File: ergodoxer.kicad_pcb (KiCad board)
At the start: 2 copper layers, 207 x 174.1 mm, 113 parts, among them J1 USB_C_Receptacle, SW1 SW_Push, SW10 SW_Push, SW11 SW_Push, SW12 SW_Push, SW13 SW_Push, SW14 SW_Push, SW15 SW_Push, SW16 SW_Push, SW17 SW_Push, SW18 SW_Push, SW19 SW_Push, SW2 SW_Push, SW20 SW_Push, SW21 SW_Push, SW22 SW_Push, SW23 SW_Push, SW24 SW_Push, SW25 SW_Push, SW26 SW_Push, SW27 SW_Push, SW28 SW_Push, SW29 SW_Push, SW3 SW_Push, SW30 SW_Push, SW31 SW_Push, SW32 SW_Push, SW33 SW_Push, SW34 SW_Push, SW35 SW_Push, SW36 SW_Push, SW37 SW_Push, SW38 SW_Push, SW39 SW_Push, SW4 SW_Push, SW40 SW_Push, SW41 SW_Push, SW43 SW_Push, SW44 SW_Push, SW45 SW_Push, SW46 SW_Push, SW47 SW_Push, SW48 SW_Push, SW49 SW_Push, SW5 SW_Push, SW50 SW_Push, SW51 SW_Push, SW52 SW_Push, SW53 SW_Push, SW6 SW_Push, SW7 SW_Push, SW8 SW_Push, SW9 SW_Push, U1 Proton_C

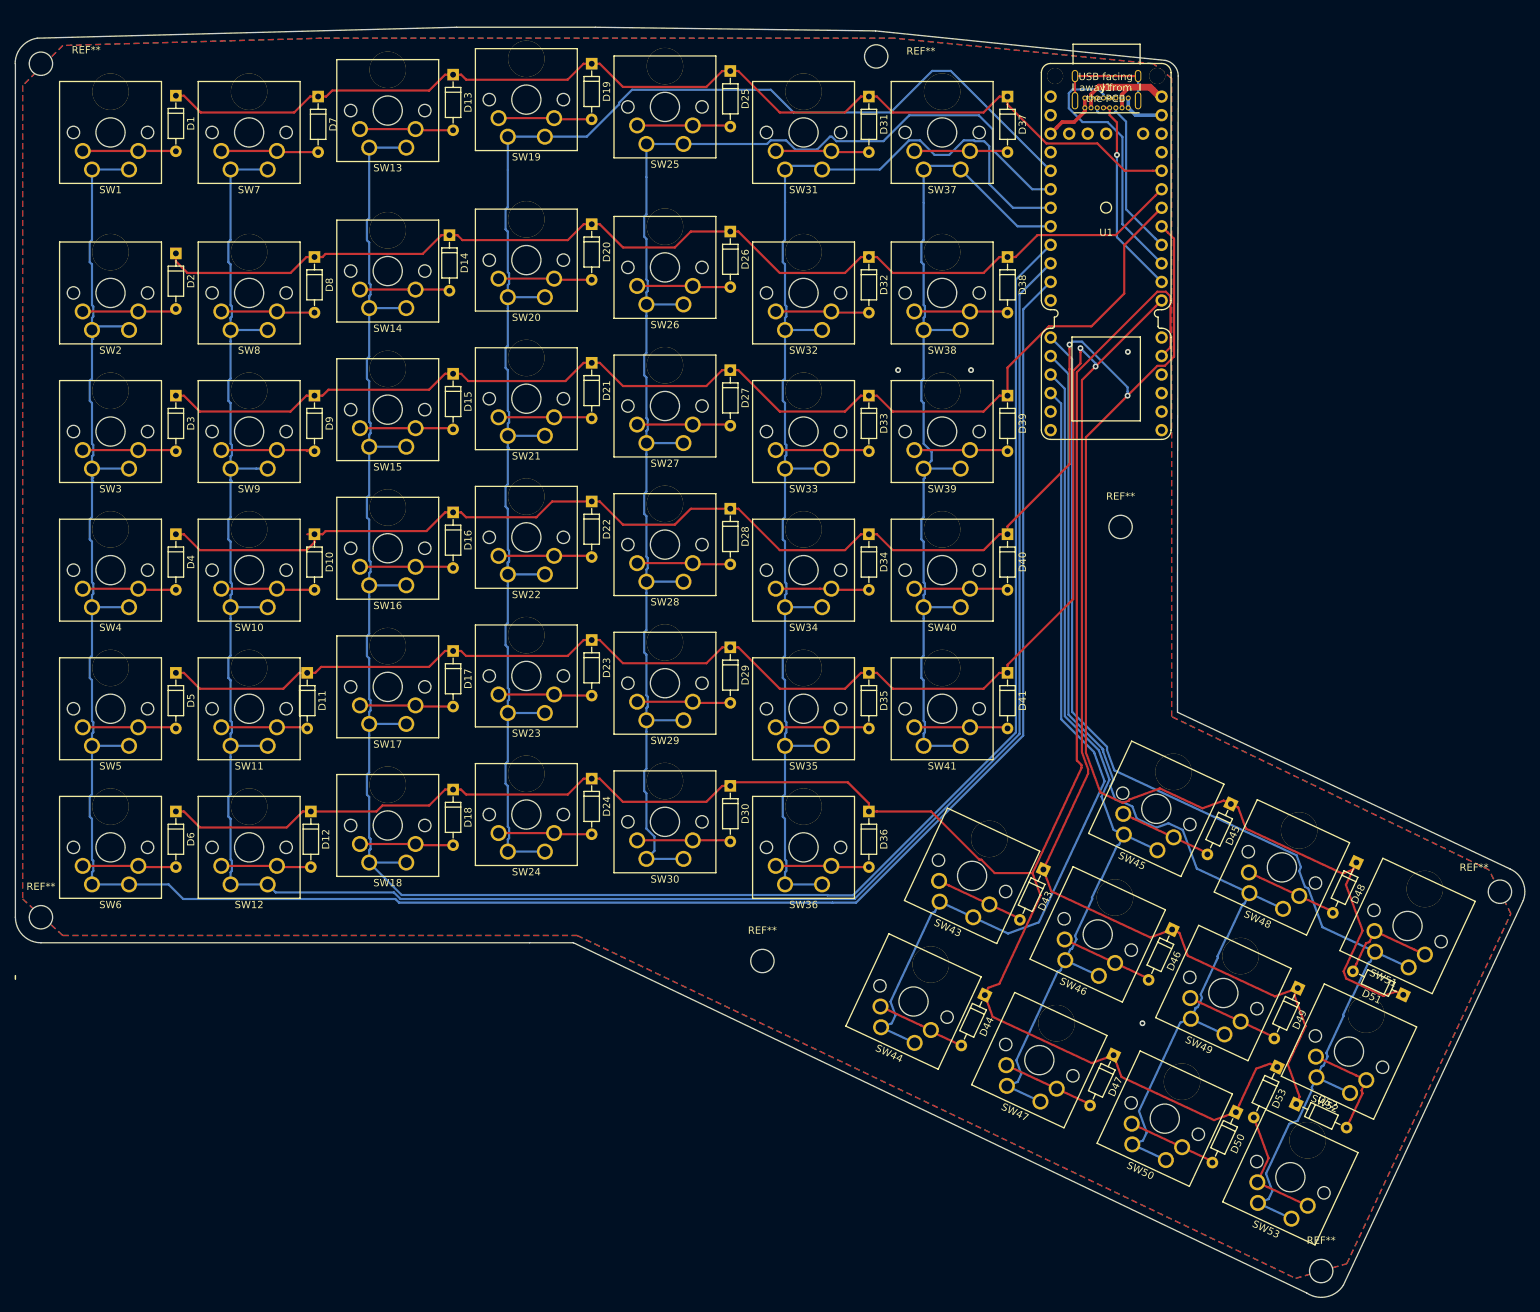
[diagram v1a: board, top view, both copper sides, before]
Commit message: Add leds
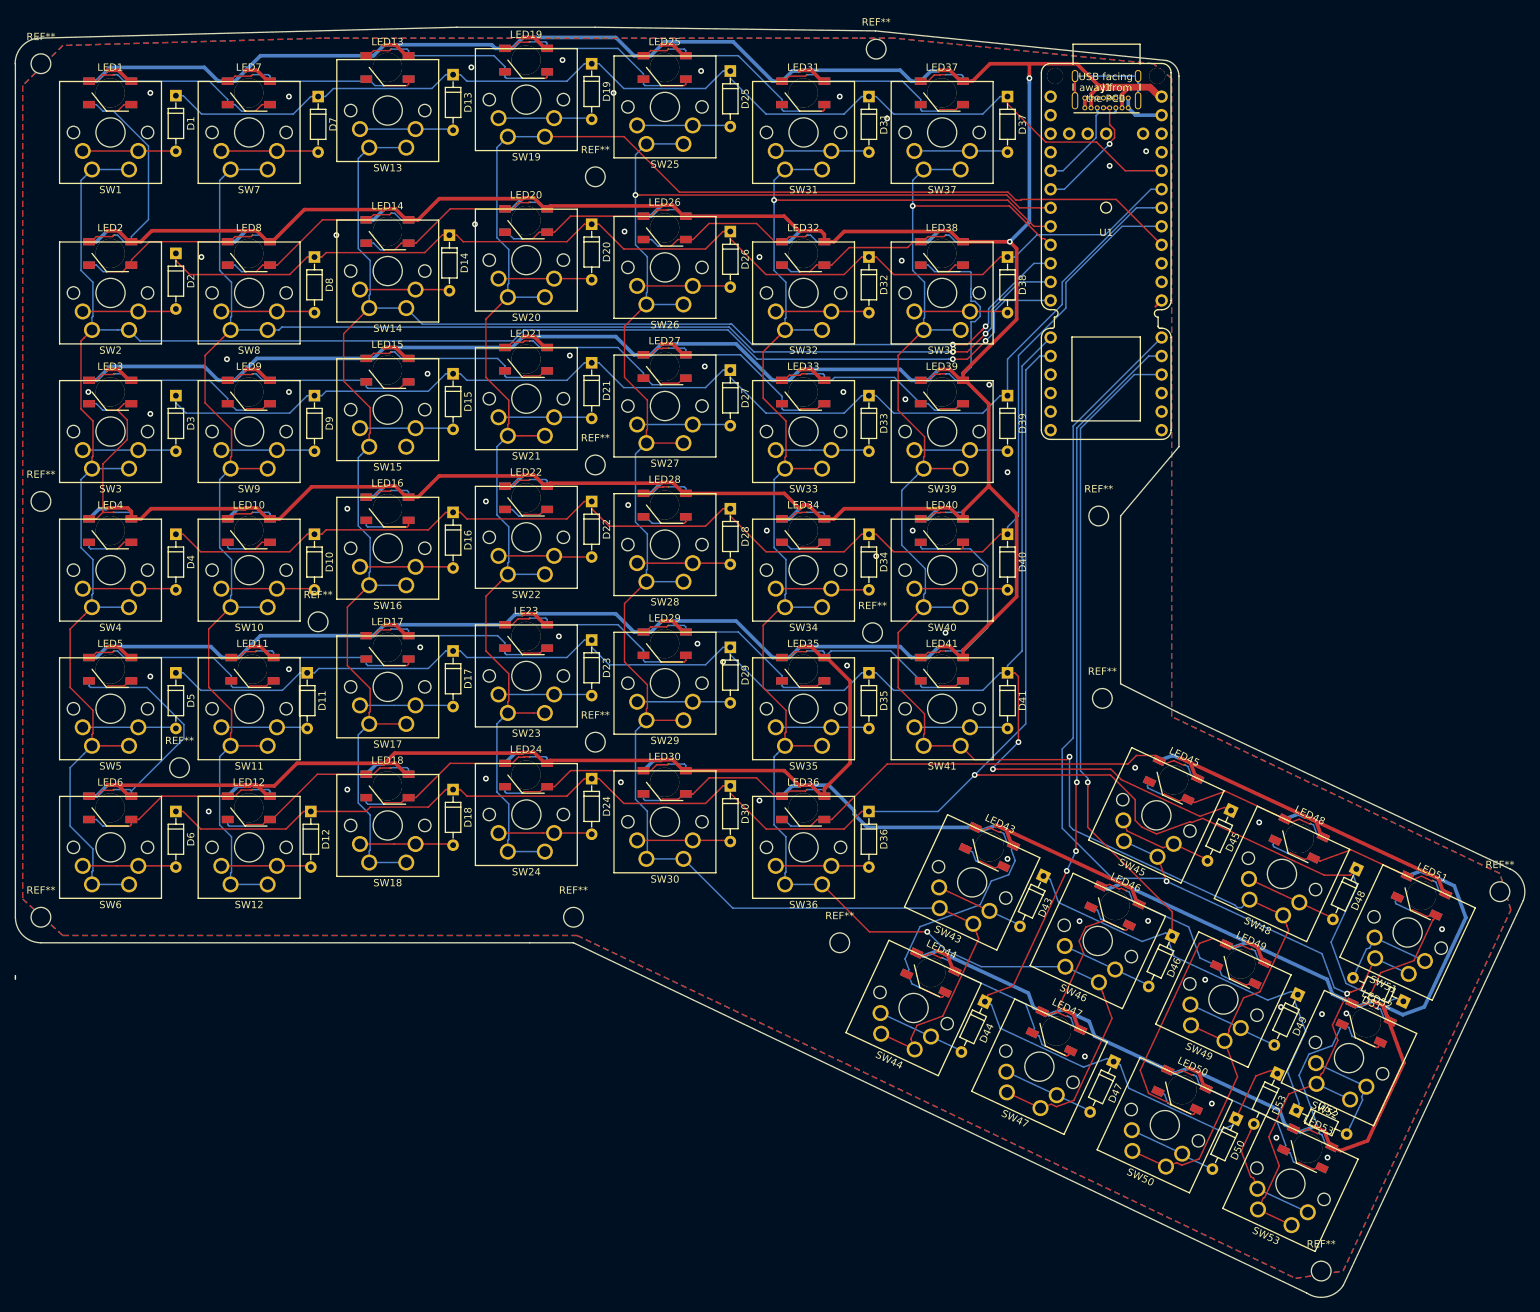
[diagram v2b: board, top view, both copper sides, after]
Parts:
- removed the REF** at (215.0, 88.0)
- removed the REF** at (181.5, 23.5)
- removed the REF** at (67.0, 24.5)
- removed the REF** at (67.0, 141.5)
- removed the REF** at (165.9, 147.5)
- removed the REF** at (242.5, 190.0)
- removed the REF** at (267.0, 138.0)
- added LE23: WS2812B, switches:LED_WS2812B-inverted, F.Cu at (133.5, 103.0)
- added LED1: WS2812B, switches:LED_WS2812B-inverted, F.Cu at (76.5, 28.5)
- added LED10: WS2812B, switches:LED_WS2812B-inverted, F.Cu at (95.5, 88.5)
- added LED11: WS2812B, switches:LED_WS2812B-inverted, F.Cu at (96.0, 107.5)
- added LED12: WS2812B, switches:LED_WS2812B-inverted, F.Cu at (95.5, 126.5)
- added LED13: WS2812B, switches:LED_WS2812B-inverted, F.Cu at (114.5, 25.0)
- added LED14: WS2812B, switches:LED_WS2812B-inverted, F.Cu at (114.5, 47.5)
- added LED15: WS2812B, switches:LED_WS2812B-inverted, F.Cu at (114.5, 66.5)
- added LED16: WS2812B, switches:LED_WS2812B-inverted, F.Cu at (114.5, 85.5)
- added LED17: WS2812B, switches:LED_WS2812B-inverted, F.Cu at (114.5, 104.5)
- added LED18: WS2812B, switches:LED_WS2812B-inverted, F.Cu at (114.5, 123.5)
- added LED19: WS2812B, switches:LED_WS2812B-inverted, F.Cu at (133.5, 24.0)
- added LED2: WS2812B, switches:LED_WS2812B-inverted, F.Cu at (76.5, 50.5)
- added LED20: WS2812B, switches:LED_WS2812B-inverted, F.Cu at (133.5, 46.0)
- added LED21: WS2812B, switches:LED_WS2812B-inverted, F.Cu at (133.5, 65.0)
- added LED22: WS2812B, switches:LED_WS2812B-inverted, F.Cu at (133.5, 84.0)
- added LED24: WS2812B, switches:LED_WS2812B-inverted, F.Cu at (133.5, 122.0)
- added LED25: WS2812B, switches:LED_WS2812B-inverted, F.Cu at (152.5, 25.0)
- added LED26: WS2812B, switches:LED_WS2812B-inverted, F.Cu at (152.5, 47.0)
- added LED27: WS2812B, switches:LED_WS2812B-inverted, F.Cu at (152.5, 66.0)
- added LED28: WS2812B, switches:LED_WS2812B-inverted, F.Cu at (152.5, 85.0)
- added LED29: WS2812B, switches:LED_WS2812B-inverted, F.Cu at (152.5, 104.0)
- added LED3: WS2812B, switches:LED_WS2812B-inverted, F.Cu at (76.5, 69.5)
- added LED30: WS2812B, switches:LED_WS2812B-inverted, F.Cu at (152.5, 123.0)
- added LED31: WS2812B, switches:LED_WS2812B-inverted, F.Cu at (171.5, 28.5)
- added LED32: WS2812B, switches:LED_WS2812B-inverted, F.Cu at (171.5, 50.5)
- added LED33: WS2812B, switches:LED_WS2812B-inverted, F.Cu at (171.5, 69.5)
- added LED34: WS2812B, switches:LED_WS2812B-inverted, F.Cu at (171.5, 88.5)
- added LED35: WS2812B, switches:LED_WS2812B-inverted, F.Cu at (171.5, 107.5)
- added LED36: WS2812B, switches:LED_WS2812B-inverted, F.Cu at (171.5, 126.5)
- added LED37: WS2812B, switches:LED_WS2812B-inverted, F.Cu at (190.5, 28.5)
- added LED38: WS2812B, switches:LED_WS2812B-inverted, F.Cu at (190.5, 50.5)
- added LED39: WS2812B, switches:LED_WS2812B-inverted, F.Cu at (190.5, 69.5)
- added LED4: WS2812B, switches:LED_WS2812B-inverted, F.Cu at (76.5, 88.5)
- added LED40: WS2812B, switches:LED_WS2812B-inverted, F.Cu at (190.5, 88.5)
- added LED41: WS2812B, switches:LED_WS2812B-inverted, F.Cu at (190.5, 107.5)
- added LED43: WS2812, switches:LED_WS2812B-inverted, F.Cu at (197.0, 131.9)
- added LED44: WS2812, switches:LED_WS2812B-inverted, F.Cu at (189.0, 149.1)
- added LED45: WS2812B, switches:LED_WS2812B-inverted, F.Cu at (222.3, 122.7)
- added LED46: WS2812B, switches:LED_WS2812B-inverted, F.Cu at (214.2, 139.9)
- added LED47: WS2812B, switches:LED_WS2812B-inverted, F.Cu at (206.2, 157.1)
- added LED48: WS2812B, switches:LED_WS2812B-inverted, F.Cu at (239.5, 130.7)
- added LED49: WS2812B, switches:LED_WS2812B-inverted, F.Cu at (231.5, 147.9)
- added LED5: WS2812B, switches:LED_WS2812B-inverted, F.Cu at (76.5, 107.5)
- added LED50: WS2812B, switches:LED_WS2812B-inverted, F.Cu at (223.4, 165.1)
- added LED51: WS2812B, switches:LED_WS2812B-inverted, F.Cu at (256.3, 138.5)
- added LED52: WS2812B, switches:LED_WS2812B-inverted, F.Cu at (248.7, 156.0)
- added LED53: WS2812B, switches:LED_WS2812B-inverted, F.Cu at (240.6, 173.2)
- added LED6: WS2812B, switches:LED_WS2812B-inverted, F.Cu at (76.5, 126.5)
- added LED7: WS2812B, switches:LED_WS2812B-inverted, F.Cu at (95.5, 28.5)
- added LED8: WS2812B, switches:LED_WS2812B-inverted, F.Cu at (95.5, 50.5)
- added LED9: WS2812B, switches:LED_WS2812B-inverted, F.Cu at (95.5, 69.5)
- added REF**: MountingHole_2.7mm, Mounting_Holes:MountingHole_2.7mm, F.Cu at (212.5, 111.5)
- added REF**: MountingHole_2.7mm, Mounting_Holes:MountingHole_2.7mm, F.Cu at (242.5, 190.0)
- added REF**: MountingHole_2.7mm, Mounting_Holes:MountingHole_2.7mm, F.Cu at (267.0, 138.0)
- added REF**: MountingHole_2.7mm, Mounting_Holes:MountingHole_2.7mm, F.Cu at (212.0, 86.5)
- added REF**: MountingHole_2.7mm, Mounting_Holes:MountingHole_2.7mm, F.Cu at (181.5, 22.5)
- added REF**: MountingHole_2.7mm, Mounting_Holes:MountingHole_2.7mm, F.Cu at (67.0, 24.5)
- added REF**: MountingHole_2.7mm, Mounting_Holes:MountingHole_2.7mm, F.Cu at (86.0, 121.0)
- added REF**: MountingHole_2.7mm, Mounting_Holes:MountingHole_2.7mm, F.Cu at (67.0, 141.5)
- added REF**: MountingHole_2.7mm, Mounting_Holes:MountingHole_2.7mm, F.Cu at (181.0, 102.5)
- added REF**: MountingHole_2.7mm, Mounting_Holes:MountingHole_2.7mm, F.Cu at (105.0, 101.0)
- added REF**: MountingHole_2.7mm, Mounting_Holes:MountingHole_2.7mm, F.Cu at (67.0, 84.5)
- added REF**: MountingHole_2.7mm, Mounting_Holes:MountingHole_2.7mm, F.Cu at (143.0, 40.0)
- added REF**: MountingHole_2.7mm, Mounting_Holes:MountingHole_2.7mm, F.Cu at (143.0, 79.5)
- added REF**: MountingHole_2.7mm, Mounting_Holes:MountingHole_2.7mm, F.Cu at (143.0, 117.5)
- added REF**: MountingHole_2.7mm, Mounting_Holes:MountingHole_2.7mm, F.Cu at (140.0, 141.5)
- added REF**: MountingHole_2.7mm, Mounting_Holes:MountingHole_2.7mm, F.Cu at (176.5, 145.0)
- SW1, SW13, SW19, SW25, SW31, SW37, SW7: value SW_Push -> SW_Push_mod
- U1: value Proton_C -> proton_c
- moved D49 0.89 mm to (239.3, 152.1)
- moved D43 0.89 mm to (204.4, 135.8)
- moved D48 0.89 mm to (247.3, 134.9)
- moved D50 0.89 mm to (230.8, 169.1)
- moved SW43 0.89 mm to (190.2, 140.3)
- moved SW45 0.89 mm to (215.5, 131.1)
- moved SW52 0.89 mm to (241.9, 164.3)
- moved SW47 0.89 mm to (199.4, 165.5)
- moved D47 0.89 mm to (214.0, 161.3)
- moved D44 0.89 mm to (196.4, 153.1)
- moved SW51 0.89 mm to (249.9, 147.1)
- moved D51 0.89 mm to (253.8, 153.0)
- moved SW48 0.89 mm to (232.7, 139.1)
- moved D52 0.89 mm to (239.1, 168.0)
- moved SW49 0.89 mm to (224.6, 156.3)
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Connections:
- D43 pad 1: row5 -> row7
- D44 pad 1: row6 -> row8
- D45 pad 1: row4 -> row5
- D46 pad 1: row5 -> row7
- D47 pad 1: row6 -> row8
- D48 pad 1: row4 -> row6
- D49 pad 1: row5 -> row7
- D50 pad 1: row6 -> row8
- D51 pad 1: row4 -> row6
- D52 pad 1: row5 -> row7
- D53 pad 1: row6 -> row8
- J1 pad A5: Net-(J1-PadA5) -> SDA
- J1 pad A6: Net-(J1-PadA6) -> SCL
- J1 pad A7: Net-(J1-PadA6) -> SCL
- J1 pad A8: Net-(J1-PadA5) -> SDA
- J1 pad B7: Net-(J1-PadB6) -> Net-(J1-PadB7)
- SW43 pad 1: column8 -> column5
- SW44 pad 1: column8 -> column5
- SW45 pad 1: column9 -> column8
- SW46 pad 1: column9 -> column6
- SW47 pad 1: column9 -> column6
- SW48 pad 1: column10 -> column7
- SW49 pad 1: column10 -> column7
- SW50 pad 1: column10 -> column7
- SW51 pad 1: column11 -> column8
- SW52 pad 1: column11 -> column8
- SW53 pad 1: column11 -> column8
- U1 pad A4: column11 -> row5
- U1 pad A5: column10 -> row6
- U1 pad A6: column9 -> Net-(U1-PadA6)
- U1 pad A7: column8 -> Net-(U1-PadA7)
- U1 pad B0: Net-(U1-PadB0) -> column1
- U1 pad B1: column1 -> column2
- U1 pad B10: Net-(U1-PadB10) -> column8
- U1 pad B11: row6 -> row8
- U1 pad B12: Net-(U1-PadB12) -> row7
- U1 pad B13: Net-(J1-PadA5) -> column4
- U1 pad B14: Net-(J1-PadB6) -> Net-(U1-PadB14)
- U1 pad B15: Net-(J1-PadA6) -> LED_IN
- U1 pad B2: column2 -> column3
- U1 pad B3: column3 -> column7
- U1 pad B4: column7 -> column6
- U1 pad B5: column6 -> column5
- U1 pad B6: column5 -> SCL
- U1 pad B7: column4 -> SDA
- U1 pad B9: row5 -> Net-(U1-PadB9)
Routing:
- net VBUS: track 25.6 -> 1372.2 mm, vias 0 -> 2
- net column11: track 164.3 -> 0.00 mm
- net row8: track 0.00 -> 151.0 mm, vias 0 -> 3
- net row7: track 0.00 -> 149.2 mm, vias 0 -> 1
- net column10: track 144.7 -> 0.00 mm
- net row4: track 319.6 -> 181.7 mm, vias 2 -> 0
- net column7: track 122.7 -> 246.9 mm, vias 0 -> 2
- net column9: track 122.3 -> 0.00 mm
- net row5: track 321.0 -> 226.5 mm
- net column6: track 172.0 -> 246.5 mm, vias 0 -> 2
- net column5: track 190.6 -> 264.6 mm, vias 0 -> 1
- net column8: track 117.3 -> 187.6 mm, vias 0 -> 2
- net column3: track 299.4 -> 230.6 mm, vias 0 -> 2
- net Net-(LED36-Pad2): track 0.00 -> 62.9 mm
- net column1: track 329.8 -> 272.0 mm, vias 0 -> 2
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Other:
- outline, holes or cut-outs redrawn
- net class Default: trace_width 0.3 -> 0.2

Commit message: WIP update to square led holes
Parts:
- removed D36: 1N4148, Diodes_ThroughHole:D_DO-35_SOD27_P7.62mm_Horizontal
- removed LED36: WS2812B, switches:LED_WS2812B-inverted
- removed REF** (x16): MountingHole_2.7mm, Mounting_Holes:MountingHole_2.7mm
- removed SW36: SW_Push, switches:SW_Cherry_MX_1.00u_PCB_dual
- moved SW53 138.8 mm to (372.1, 169.4), turned to 180 degrees
- moved SW50 136.6 mm to (353.1, 169.4), turned to 180 degrees
- moved LED53 134.9 mm to (374.7, 159.0), turned to 0 degrees
- moved SW47 134.8 mm to (334.1, 169.4), turned to 180 degrees
- moved D50 133.7 mm to (364.1, 159.4), turned to 270 degrees
- moved SW44 133.5 mm to (315.1, 169.4), turned to 180 degrees
- moved D52 132.8 mm to (371.1, 154.0), turned to 0 degrees
- moved LED50 132.5 mm to (355.7, 159.0), turned to 0 degrees
- moved D47 131.6 mm to (345.6, 159.4), turned to 270 degrees
- moved SW52 131.0 mm to (372.1, 150.4), turned to 180 degrees
- moved D53 130.7 mm to (366.6, 151.4), turned to 270 degrees
- moved LED47 130.6 mm to (336.7, 159.0), turned to 0 degrees
- moved D44 129.9 mm to (326.1, 159.4), turned to 270 degrees
- moved LED44 129.1 mm to (317.7, 159.0), turned to 0 degrees
- moved SW49 128.6 mm to (353.1, 150.4), turned to 180 degrees
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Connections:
- D45 pad 1: row5 -> row6
- LED16 pad 4: Net-(LED16-Pad4) -> Net-(LED10-Pad2)
- LED22 pad 4: Net-(LED22-Pad4) -> Net-(LED16-Pad2)
- LED28 pad 4: Net-(LED28-Pad4) -> Net-(LED22-Pad2)
- LED34 pad 4: Net-(LED34-Pad4) -> Net-(LED28-Pad2)
- LED4 pad 2: Net-(LED4-Pad2) -> Net-(LED10-Pad4)
- LED40 pad 4: Net-(LED40-Pad4) -> Net-(LED34-Pad2)
- LED45 pad 4: Net-(LED36-Pad2) -> Net-(LED30-Pad2)
- SW45 pad 1: column8 -> column6
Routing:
- net row6: track 270.5 -> 177.9 mm, vias 1 -> 0
- net column8: track 187.6 -> 104.5 mm, vias 2 -> 0
- net row7: track 149.2 -> 73.9 mm
- net row5: track 226.5 -> 151.4 mm, vias 2 -> 0
- net row8: track 151.0 -> 87.9 mm, vias 3 -> 2
- net Net-(LED36-Pad2): track 62.9 -> 0.00 mm
- net VBUS: track 1372.2 -> 1407.9 mm, vias 2 -> 0
- net row1: track 153.0 -> 184.5 mm
- net column6: track 246.5 -> 215.1 mm
- net column7: track 246.9 -> 215.9 mm
- net row4: track 181.7 -> 150.9 mm
- net Net-(LED10-Pad2): track 6.96 -> 32.0 mm
- net Net-(LED28-Pad2): track 6.96 -> 31.4 mm
- net Net-(LED34-Pad2): track 6.55 -> 30.8 mm
- net Net-(LED16-Pad2): track 7.37 -> 31.4 mm
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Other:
- board size 207 x 174.1 mm -> 313.8 x 174.1 mm

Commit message: Add switches lib
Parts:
- U1: value proton_c -> Proton_C
